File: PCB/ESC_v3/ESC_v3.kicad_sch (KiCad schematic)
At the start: 80 parts, among them J1 Conn_01x04_Pin, J11 Screw_Terminal_01x01, J2 Screw_Terminal_01x01, Q1 NTMFS2D1N08XT1G, Q2 NTMFS2D1N08XT1G, Q3 NTMFS2D1N08XT1G, Q4 NTMFS2D1N08XT1G, Q5 NTMFS2D1N08XT1G, Q6 NTMFS2D1N08XT1G, U1 SN65HVD232

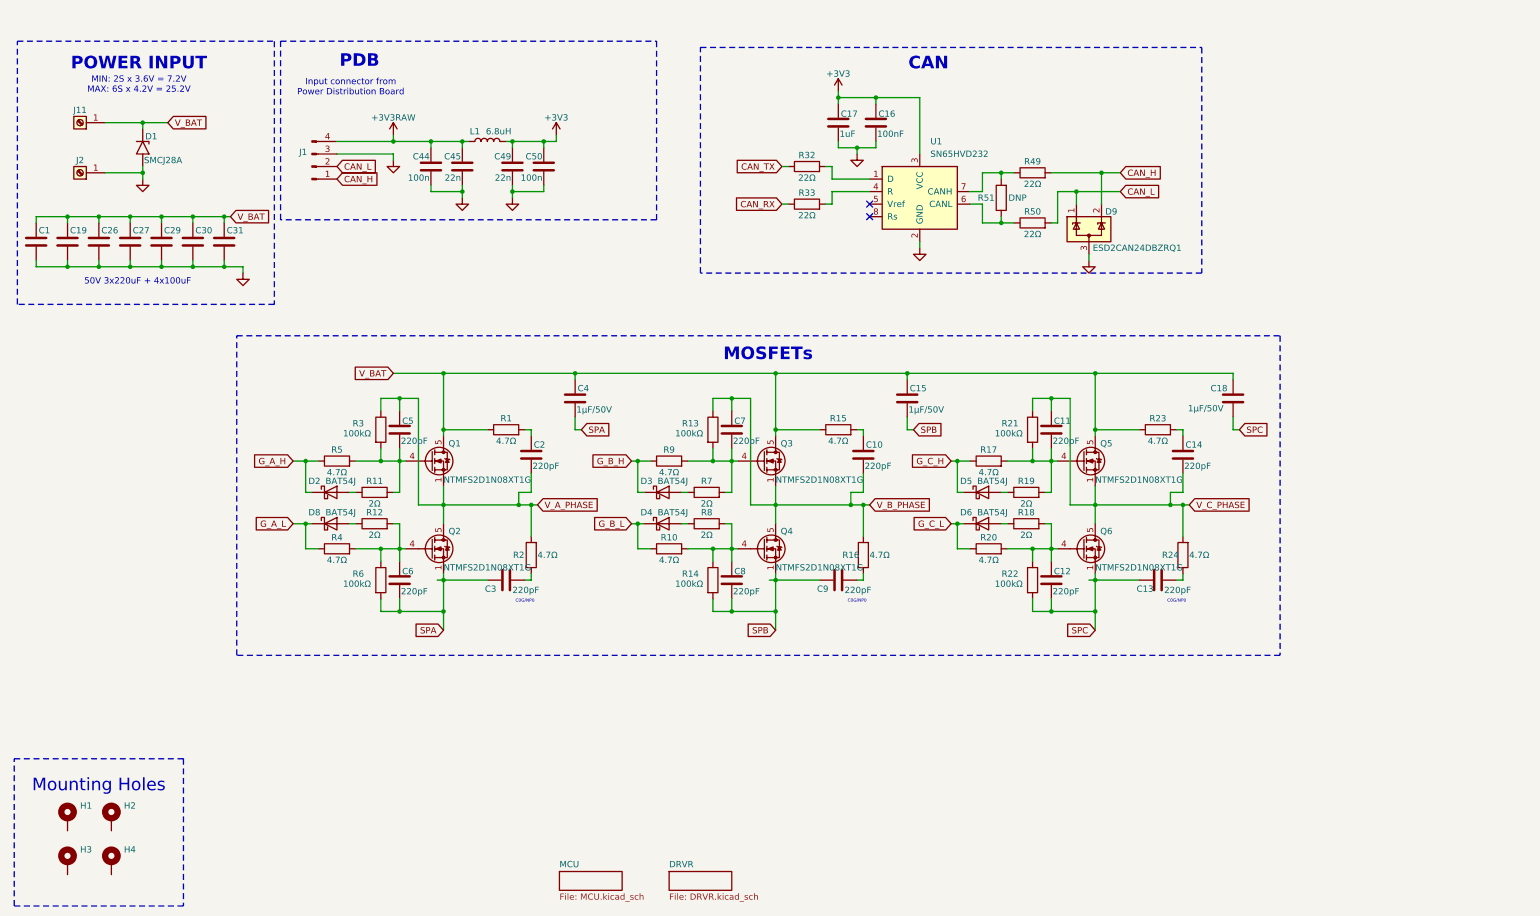
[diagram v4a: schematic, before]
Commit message: STM changed
Changed specific STM model for better pinouts and layout
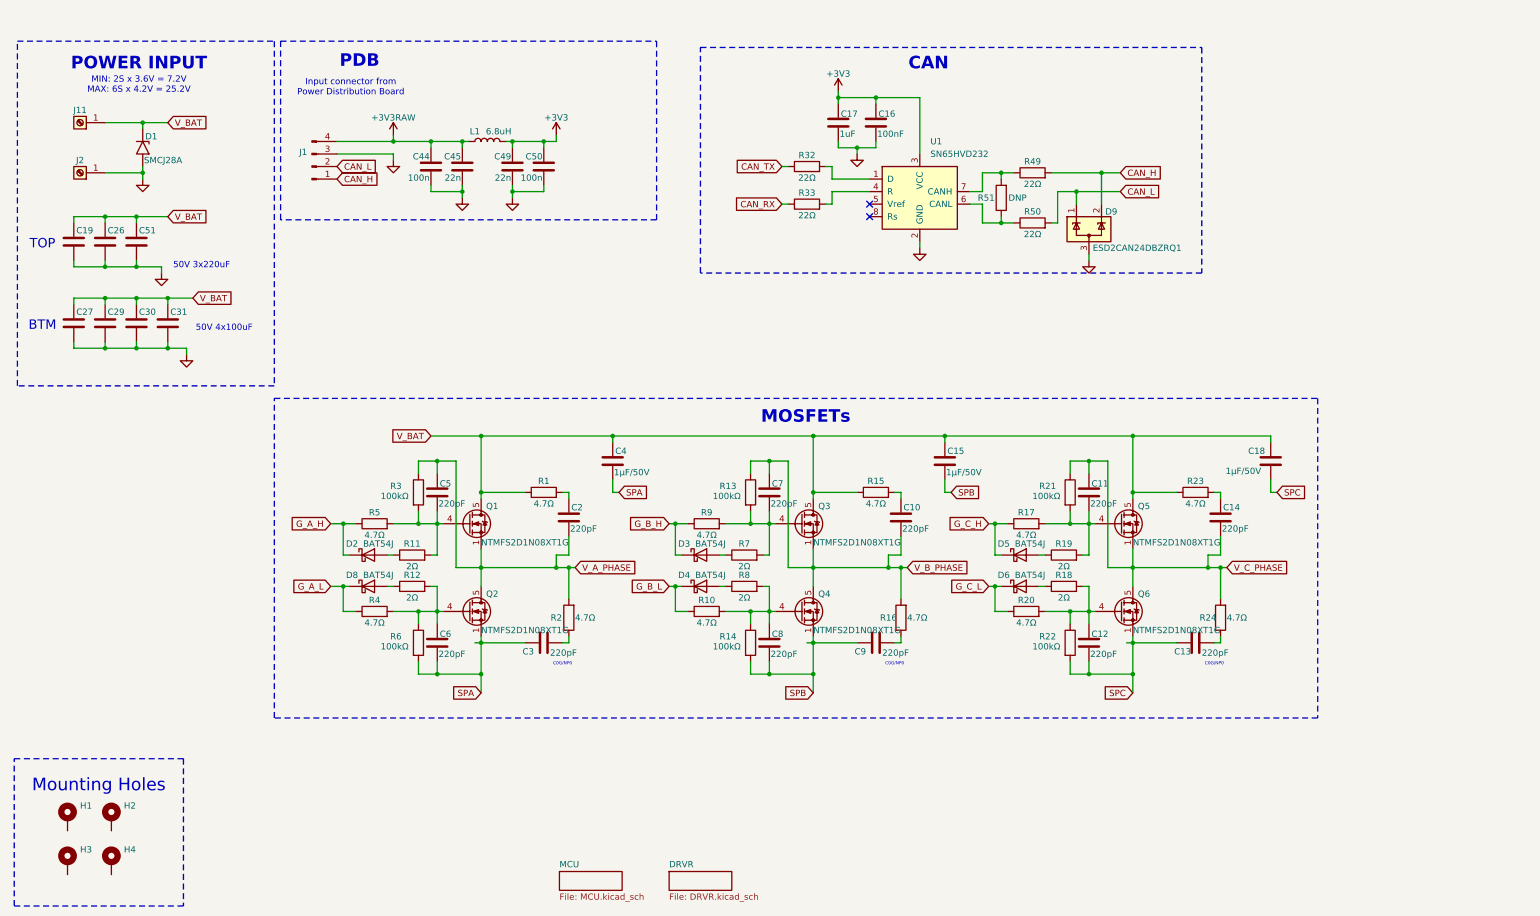
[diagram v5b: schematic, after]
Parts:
- removed C1: 100-220uF, Capacitor_SMD:C_2220_5750Metric, symbol Device:C
- added C51: 100-220uF, Capacitor_SMD:CP_Elec_8x10, symbol Device:C
- C19, C26: footprint Capacitor_SMD:C_2220_5750Metric -> Capacitor_SMD:CP_Elec_8x10
- C27, C29, C30, C31: footprint Capacitor_SMD:C_2220_5750Metric -> Capacitor_SMD:CP_Elec_6.3x7.7
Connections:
- net GND: now also C51.2
- net V_BAT: now also C51.1
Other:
- note added: "50V 3x220uF"
- note added: "50V 4x100uF"
- note added: "BTM"
- note added: "TOP"
- note removed: "50V 3x220uF + 4x100uF"
- moved on the sheet: C10, C11, C12, C13, C14, C15, C18, C19, C2, C26, C27, C29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

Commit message: Layout update
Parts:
- removed R32, R33, R49, R50: 22Ω, Resistor_SMD:R_0603_1608Metric, symbol Device:R
- added U4: TCAN334G, Package_SO:JEITA_SOIC-8_3.9x4.9mm_P1.27mm, symbol Interface_CAN_LIN:TCAN334G
- added U5: TCAN334G, Package_SO:SOIC-8_3.9x4.9mm_P1.27mm, symbol Interface_CAN_LIN:TCAN334G
- added U6: TCAN334G, Package_TO_SOT_SMD:TSOT-23-8, symbol Interface_CAN_LIN:TCAN334G
- added U7: SN65HVD232, Package_SO:SOIC-8_3.9x4.9mm_P1.27mm, symbol Interface_CAN_LIN:SN65HVD230
- R51: value DNP -> 120R/DNP
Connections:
- net CAN_H: now also R51.2, U1.7 (CANH)
- net CAN_L: now also R51.1, U1.6 (CANL)
- net CAN_RX: now also U1.4 (R)
- net CAN_TX: now also U1.1 (D)
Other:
- moved on the sheet: D9

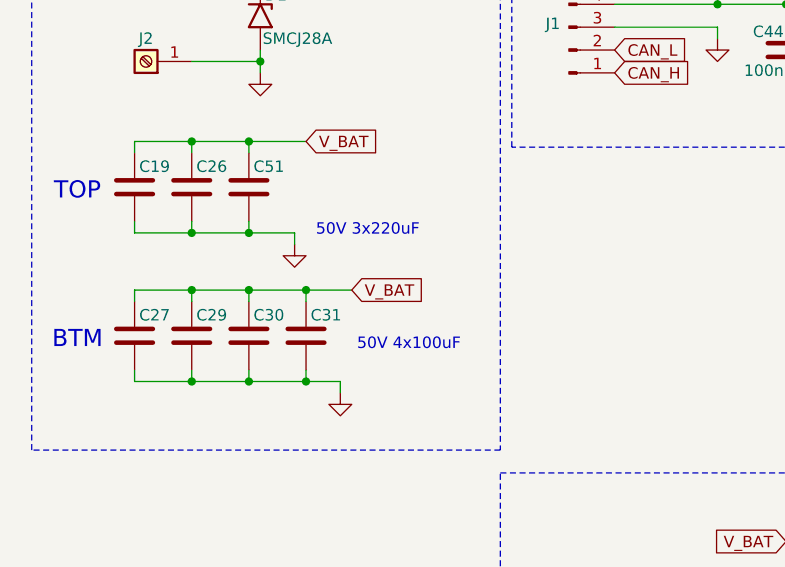
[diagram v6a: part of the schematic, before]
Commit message: Changed input connector
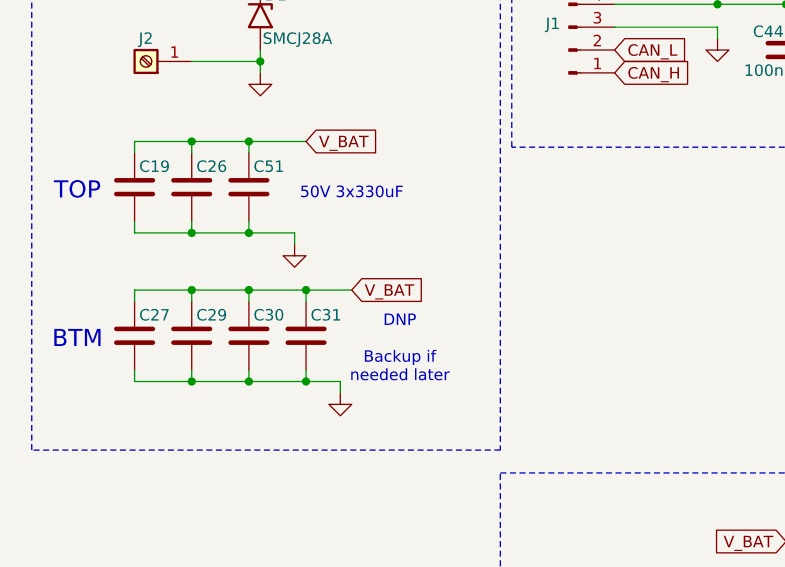
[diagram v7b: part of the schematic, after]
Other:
- note added: "50V 3x330uF"
- note added: "DNP Backup if needed later"
- note removed: "50V 3x220uF"
- note removed: "50V 4x100uF"
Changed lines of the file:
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@@
 		)
 	)
-	(text "50V 3x220uF"
+	(text "50V 3x330uF"
 		(exclude_from_sim no)
-		(at 53.848 64.516 0)
+		(at 52.07 60.452 0)
 		(effects
 			(font
@@
 		)
 	)
-	(text "50V 4x100uF"
+	(text "DNP\n\nBackup if\nneeded later"
 		(exclude_from_sim no)
-		(at 58.42 77.216 0)
+		(at 57.404 77.724 0)
 		(effects
 			(font

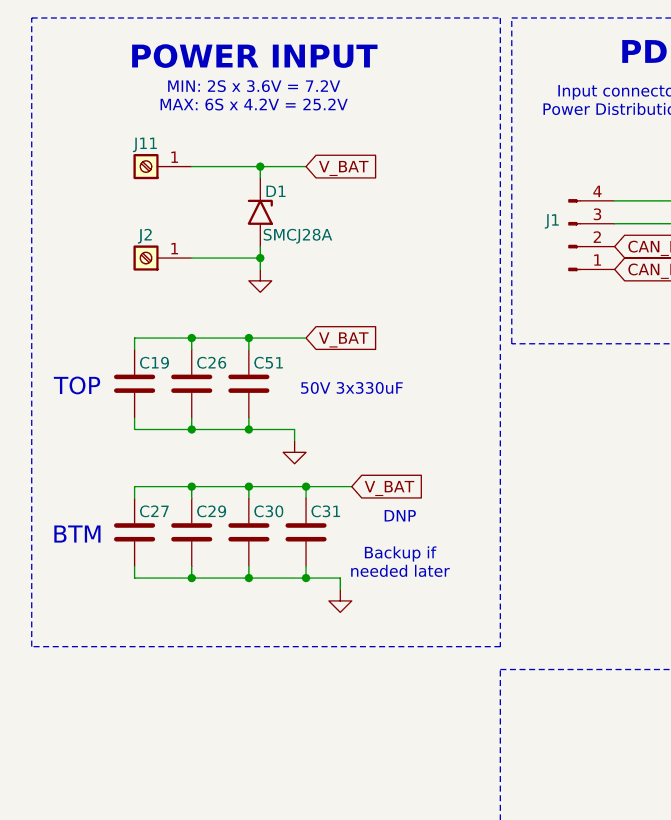
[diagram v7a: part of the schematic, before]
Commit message: Updated layout
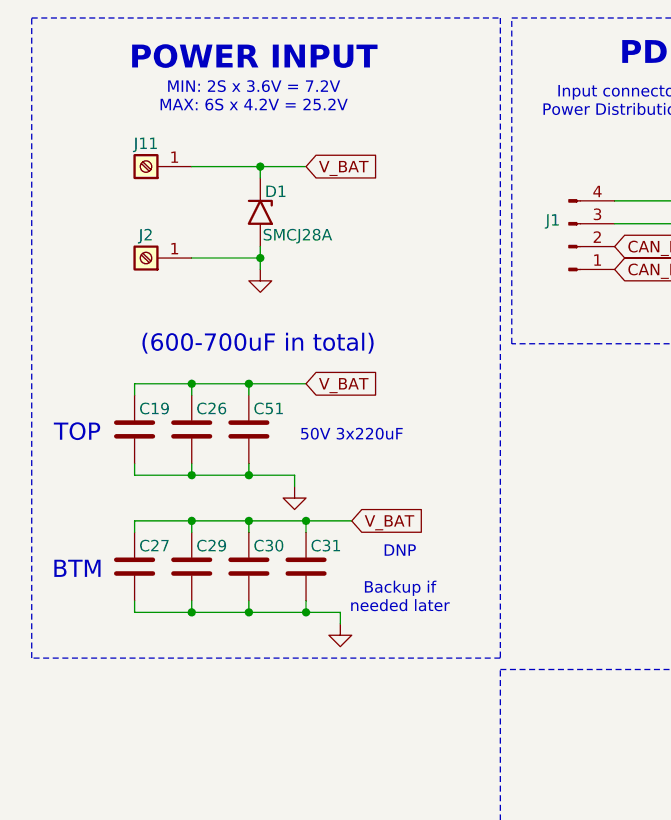
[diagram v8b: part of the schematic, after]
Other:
- note added: "(600-700uF in total)"
- note added: "50V 3x220uF"
- note removed: "50V 3x330uF"
- moved on the sheet: C19, C26, C27, C29, C30, C31, C51
